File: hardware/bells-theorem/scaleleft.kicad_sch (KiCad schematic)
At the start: 16 parts, among them U12 MCP6004

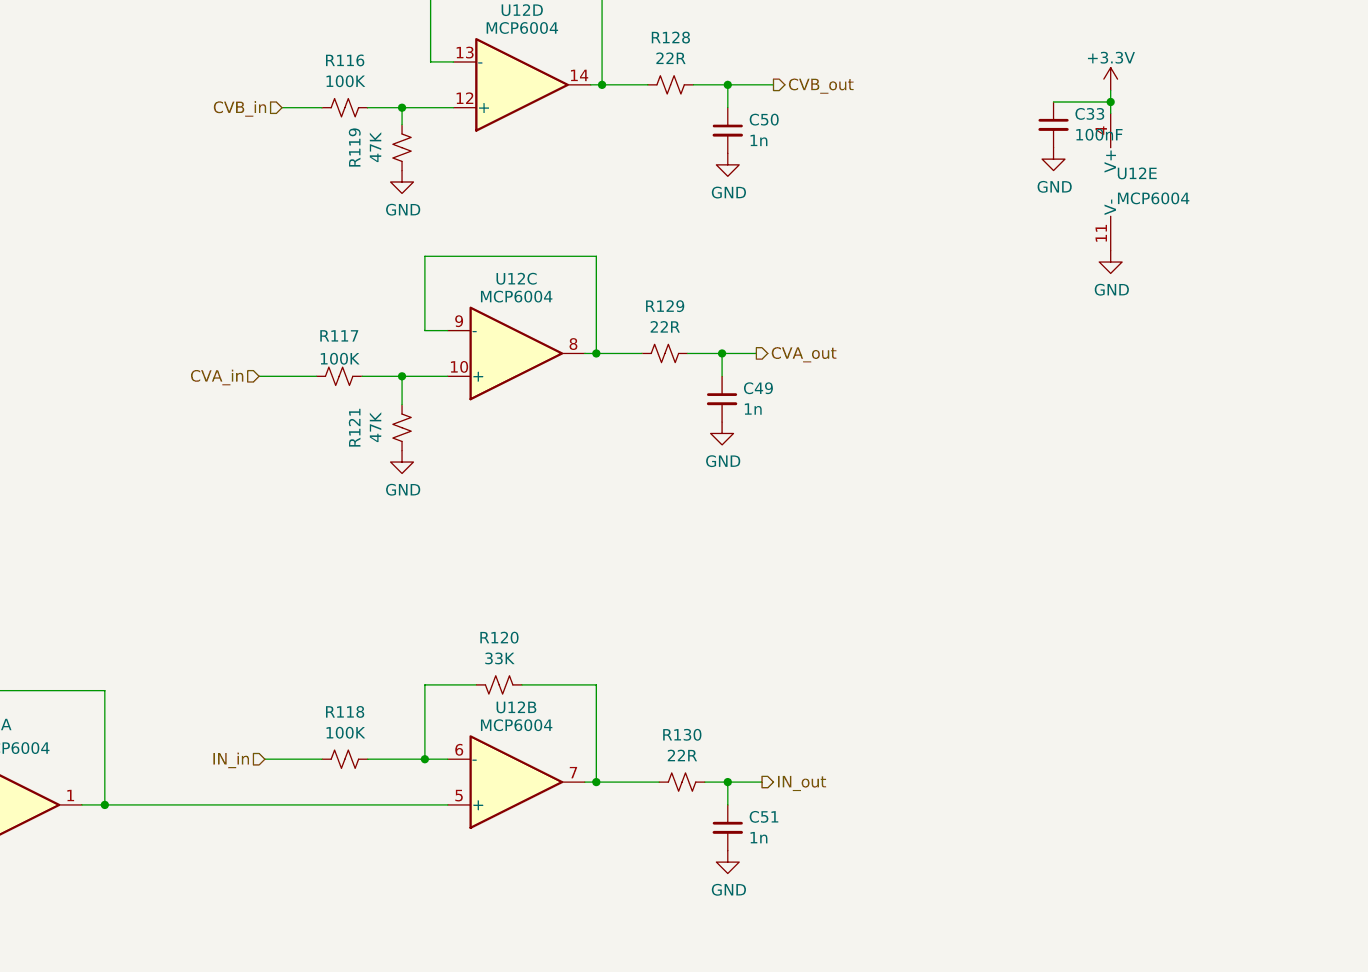
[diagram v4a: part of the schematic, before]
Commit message: current revision actually 0.6 was 1.0 candidate, but needs major revision
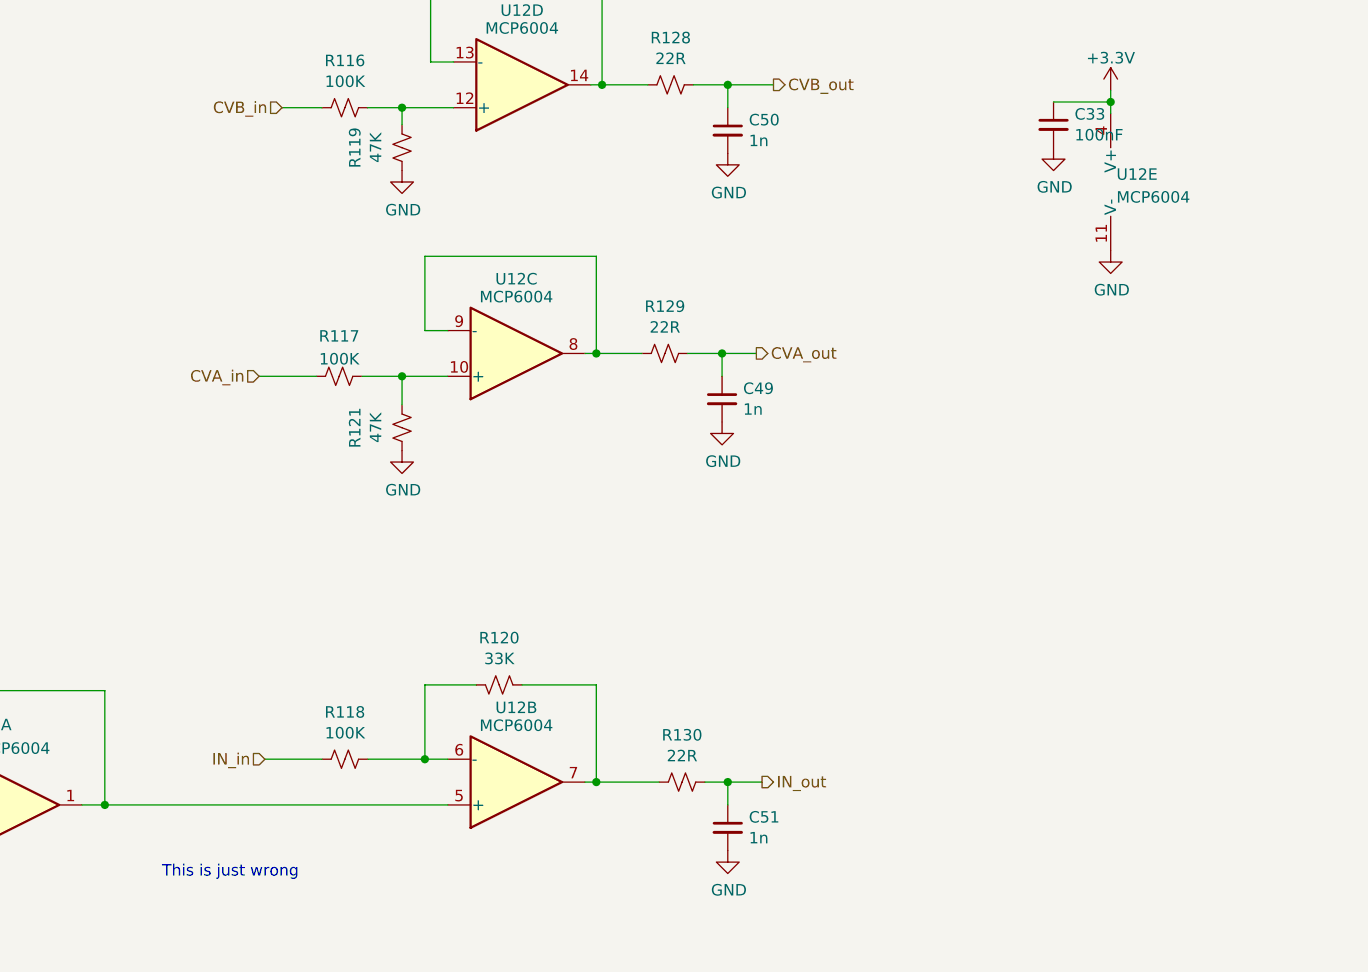
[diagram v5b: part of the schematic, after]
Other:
- note added: "This is just wrong"
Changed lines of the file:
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@@
+    (effects (font (size 1.27 1.27)) (justify left bottom))
+  )
+  (text "This is just wrong\n" (at 96.52 152.4 0)
     (effects (font (size 1.27 1.27)) (justify left bottom))
   )
@@
   (symbol (lib_id "power:GND") (at 195.58 71.12 0) (unit 1)
     (in_bom yes) (on_board yes)
-    (property "Reference" "#PWR0226" (id 0) (at 195.58 77.47 0)
+    (property "Reference" "#PWR0168" (id 0) (at 195.58 77.47 0)
       (effects (font (size 1.27 1.27)) hide)
     )
@@
   (symbol (lib_id "power:GND") (at 201.93 82.55 0) (unit 1)
     (in_bom yes) (on_board yes)
-    (property "Reference" "#PWR0227" (id 0) (at 201.93 88.9 0)
+    (property "Reference" "#PWR0170" (id 0) (at 201.93 88.9 0)
       (effects (font (size 1.27 1.27)) hide)
     )
@@
   (symbol (lib_id "power:GND") (at 158.75 101.6 0) (unit 1)
     (in_bom yes) (on_board yes)
-    (property "Reference" "#PWR059" (id 0) (at 158.75 107.95 0)
+    (property "Reference" "#PWR0165" (id 0) (at 158.75 107.95 0)
       (effects (font (size 1.27 1.27)) hide)
     )
@@
   (symbol (lib_id "power:GND") (at 159.385 71.755 0) (unit 1)
     (in_bom yes) (on_board yes)
-    (property "Reference" "#PWR060" (id 0) (at 159.385 78.105 0)
+    (property "Reference" "#PWR0166" (id 0) (at 159.385 78.105 0)
       (effects (font (size 1.27 1.27)) hide)
     )
@@
   (symbol (lib_id "power:GND") (at 159.385 149.225 0) (unit 1)
     (in_bom yes) (on_board yes)
-    (property "Reference" "#PWR061" (id 0) (at 159.385 155.575 0)
+    (property "Reference" "#PWR0167" (id 0) (at 159.385 155.575 0)
       (effects (font (size 1.27 1.27)) hide)
     )
@@
   (symbol (lib_id "power:+3.3V") (at 201.93 64.77 0) (unit 1)
     (in_bom yes) (on_board yes) (fields_autoplaced)
-    (property "Reference" "#PWR073" (id 0) (at 201.93 68.58 0)
+    (property "Reference" "#PWR0169" (id 0) (at 201.93 68.58 0)
       (effects (font (size 1.27 1.27)) hide)
     )
@@
   (symbol (lib_id "power:GND") (at 123.19 73.66 0) (unit 1)
     (in_bom yes) (on_board yes)
-    (property "Reference" "#PWR0128" (id 0) (at 123.19 80.01 0)
+    (property "Reference" "#PWR0163" (id 0) (at 123.19 80.01 0)
       (effects (font (size 1.27 1.27)) hide)
     )
@@
   (symbol (lib_id "power:GND") (at 65.405 154.94 0) (unit 1)
     (in_bom yes) (on_board yes)
-    (property "Reference" "#PWR072" (id 0) (at 65.405 161.29 0)
+    (property "Reference" "#PWR0162" (id 0) (at 65.405 161.29 0)
       (effects (font (size 1.27 1.27)) hide)
     )
@@
   (symbol (lib_id "power:+3.3V") (at 65.405 139.7 0) (unit 1)
     (in_bom yes) (on_board yes) (fields_autoplaced)
-    (property "Reference" "#PWR071" (id 0) (at 65.405 143.51 0)
+    (property "Reference" "#PWR0161" (id 0) (at 65.405 143.51 0)
       (effects (font (size 1.27 1.27)) hide)
     )
@@
   (symbol (lib_id "Amplifier_Operational:MCP6004") (at 204.47 74.93 0) (unit 5)
     (in_bom yes) (on_board yes) (fields_autoplaced)
-    (property "Reference" "U12" (id 0) (at 202.565 74.0215 0)
-      (effects (font (size 1.27 1.27)) (justify left))
-    )
-    (property "Value" "MCP6004" (id 1) (at 202.565 76.7966 0)
+    (property "Reference" "U12" (id 0) (at 202.565 74.0953 0)
+      (effects (font (size 1.27 1.27)) (justify left))
+    )
+    (property "Value" "MCP6004" (id 1) (at 202.565 76.6322 0)
       (effects (font (size 1.27 1.27)) (justify left))
     )
@@
   (symbol (lib_id "power:GND") (at 123.19 104.775 0) (unit 1)
     (in_bom yes) (on_board yes)
-    (property "Reference" "#PWR0165" (id 0) (at 123.19 111.125 0)
-      (effects (font (size 1.27 1.27)) hide)
-    )
+    (property "Reference" "#PWR0164" (id 0) (at 123.19 111.125 0)
+      (effects (font (size 1.27 1.27)) hide)
+    )

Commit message: checking in old outstanding changes prior to debugging with Claude Code
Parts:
- added R142, R143: 300K, Resistor_SMD:R_0805_2012Metric_Pad1.20x1.40mm_HandSolder, symbol Device:R_Small_US
- added R144, R145: 100K, Resistor_SMD:R_0805_2012Metric_Pad1.20x1.40mm_HandSolder, symbol Device:R_Small_US
- R10: value 20K -> 300K
- R116, R117, R118: value 100K -> 300K
- R119, R121: value 47K -> 100K
- R12: value 12K -> 100K
- R120: value 33K -> 100K
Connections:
- net +3V3: no longer R10.1
- net CVA_in: now also R142.2; no longer R117.2
- net CVB_in: now also R143.2; no longer R116.2
- net GND: now also U12.5 (+)
- net at R116.1, R119.1: now also U12.10 (+); no longer U12.12 (+)
- net at R117.1, R121.1: now also U12.12 (+); no longer U12.10 (+)
- net at R118.1, R120.1: now also U12.2 (-); no longer U12.6 (-)
- net at R120.2, R130.2: now also U12.1; no longer U12.7
- net at R10.2, R12.1: now also U12.3 (+); no longer U12.3 (+)
- new net: R129.2, R144.1, U12.14
- new net: R128.2, R145.1, U12.8
- new net: U12.6 (-), U12.7
- new net: R143.1, R145.2, U12.9 (-)
- new net: R142.1, R144.2, U12.13 (-)
- new net +5V: R10.1, R116.2, R117.2
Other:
- note added: "but remember! it's inverted, so software needs to invert it back"
- note added: "scales -5V to +5V to 0 - 3.3V"
- note added: "will need to invert in software again before sending out"
- note removed: "This is just wrong"
- moved on the sheet: C50, C51, R10, R116, R117, R118, R12, R120, R121, R128, R130, U12A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
